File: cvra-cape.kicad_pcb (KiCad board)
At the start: 2 copper layers, 160 parts, among them Q1 MBT3904DW1T1, Q2 MBT3904DW1T1, Q3 MBT3904DW1T1, Q4 MBT3904DW1T1, Q5 MBT3904DW1T1, SW1 MicroSwitch, SW10 MicroSwitch, SW11 MicroSwitch, SW12 MicroSwitch, SW13 MicroSwitch, SW14 MicroSwitch, SW15 MicroSwitch, SW16 MicroSwitch, SW2 MicroSwitch, SW3 MicroSwitch, SW4 MicroSwitch, SW5 MicroSwitch, SW6 MicroSwitch, SW7 MicroSwitch, SW8 MicroSwitch, SW9 MicroSwitch, U1 BEAGLEBONE, U2 MCP2515_TSSOP, U3 SN65HVD256, U4 SN65HVD256, U5 BQ32000, U6 PCA9685, U7 LTC4362, X1 8Mhz, X2 32768Hz

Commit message: Place components on PCB
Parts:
- added G***: LOGO, _logo:CVRA-logo-big, F.Cu at (155.3, 103.4)
- BT1: moved to B.Cu
- U2: footprint Housings_SSOP:TSSOP-20_4.4x6.5mm_Pitch0.65mm -> _std:TSSOP20
- U6: footprint Housings_SSOP:TSSOP-28_4.4x9.7mm_Pitch0.65mm -> _std:TSSOP28
- moved R15 119.6 mm to (103.0, 71.0)
- moved C7 119.4 mm to (103.0, 68.1), turned to 180 degrees
- moved R18 117.8 mm to (106.0, 69.5)
- moved R26 116.5 mm to (109.0, 69.5)
- moved CONN7 115.4 mm to (103.0, 74.0), turned to 270 degrees
- moved R25 115.3 mm to (109.0, 71.0)
- moved C8 112.7 mm to (106.0, 68.1), turned to 180 degrees
- moved C10 112.1 mm to (112.0, 68.1), turned to 180 degrees
- moved C9 111.0 mm to (109.0, 68.1), turned to 180 degrees
- moved R17 110.5 mm to (106.0, 71.0)
- moved R28 109.3 mm to (111.9, 69.5)
- moved R16 108.1 mm to (103.0, 69.5)
- moved R33 107.5 mm to (126.9, 105.5)
- moved C12 106.9 mm to (118.0, 68.1), turned to 180 degrees
- moved C11 106.8 mm to (115.0, 68.1), turned to 180 degrees
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- renumbered CONN21 to 0, CONN22 to 1, CONN35 to 10, CONN36 to 11, CONN39 to 12, CONN23 to 2, CONN24 to 3, CONN27 to 4, CONN28 to 5, CONN29 to 6, CONN30 to 7, CONN33 to 8, CONN34 to 9
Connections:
- Q1 pad 6: Net-(Q1-Pad6) -> Net-(CONN18-Pad2)
- X2 pad 2: GND -> Net-(C16-Pad1)
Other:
- board outline added: 86.4 x 54.6 mm

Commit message: Routing
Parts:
- moved C3 8.40 mm to (114.8, 83.9), turned to 0 degrees
- moved C1 8.37 mm to (114.8, 92.3), turned to 180 degrees
- moved C10 6.10 mm to (118.0, 68.1)
- moved R27 6.10 mm to (118.0, 71.0), turned to 180 degrees
- moved R28 6.10 mm to (118.0, 69.5)
- moved CONN10 6.10 mm to (118.0, 74.0)
- moved C9 3.11 mm to (105.9, 68.1)
- moved R25 3.11 mm to (105.9, 71.0), turned to 180 degrees
- moved R26 3.11 mm to (105.9, 69.5)
- moved CONN9 3.11 mm to (105.9, 74.0)
- moved R37 3.05 mm to (114.9, 71.0), turned to 180 degrees
- moved C11 3.05 mm to (112.0, 68.1)
- moved C12 3.05 mm to (114.9, 68.1)
- moved CONN11 3.05 mm to (112.0, 74.0)
- moved R35 3.05 mm to (111.9, 71.0), turned to 180 degrees
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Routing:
- net GND: track 0.00 -> 244.4 mm, vias 0 -> 49
- net +5V: track 0.00 -> 96.0 mm, vias 0 -> 5
- net /I2C2_SCL: track 0.00 -> 93.5 mm, vias 0 -> 3
- net /I2C2_SDA: track 0.00 -> 91.0 mm, vias 0 -> 3
- net /V_CAN_BUS: track 0.00 -> 88.5 mm, vias 0 -> 6
- net /PWMGEN_OE: track 0.00 -> 49.5 mm, vias 0 -> 2
- net /CAN1_SILENT: track 0.00 -> 43.4 mm, vias 0 -> 1
- net +3V3: track 0.00 -> 42.9 mm, vias 0 -> 7
- net /D_IN_20: track 0.00 -> 42.2 mm, vias 0 -> 1
- net /Actuators/POWER: track 0.00 -> 37.6 mm
- net /D_IN_18: track 0.00 -> 36.9 mm, vias 0 -> 1
- net /D_IN_19: track 0.00 -> 36.3 mm, vias 0 -> 1
- net /D_IN_17: track 0.00 -> 34.6 mm, vias 0 -> 1
- net /SPI_CAN_MOSI: track 0.00 -> 34.2 mm, vias 0 -> 1
- net /SPI_CAN_SCK: track 0.00 -> 33.7 mm, vias 0 -> 1
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- added copper zone on F.Cu, net +3V3
- added copper zone on B.Cu, net GND
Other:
- net class Default: clearance 0.2 -> 0.15; trace_width 0.25 -> 0.2
- rule trace_clearance: 0.2 -> 0.15

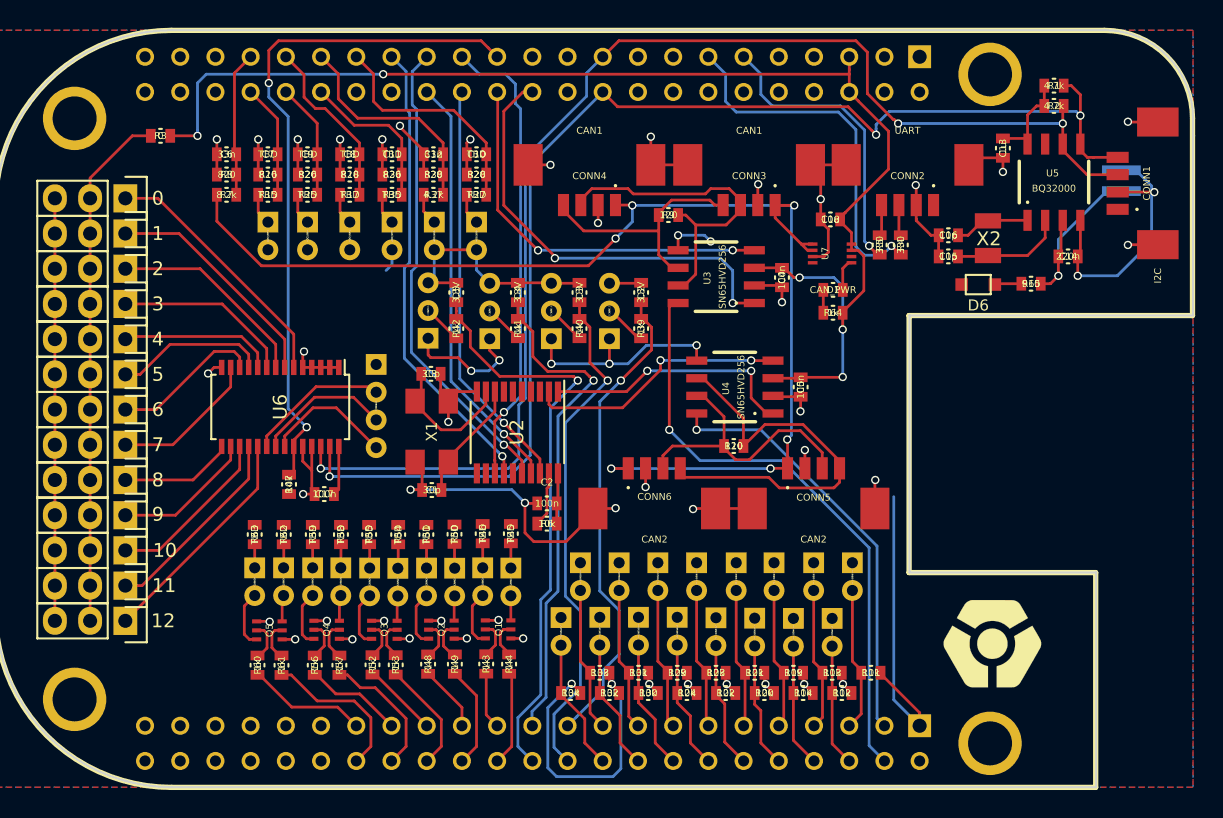
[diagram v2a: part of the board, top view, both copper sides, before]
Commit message: Routing corrections
- Use GND plane on both sides
- Route power lines as 0.5mm thickness tracks
- Cleanup crystals wiring (symetry)
- Cleanup ADC wiring to avoid crosstalk
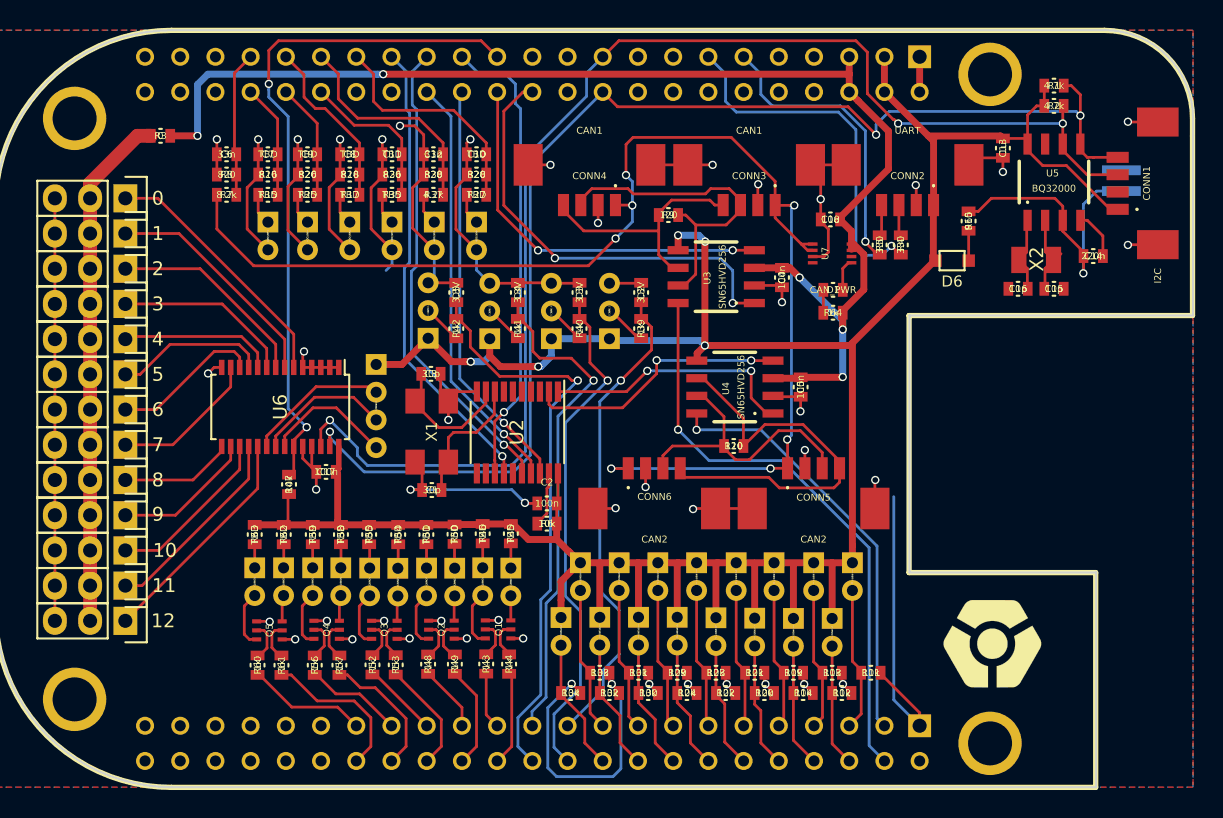
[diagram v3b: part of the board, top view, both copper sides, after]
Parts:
- moved C15 7.97 mm to (159.7, 77.8), turned to 0 degrees
- moved R65 6.38 mm to (153.5, 72.9), turned to 90 degrees
- moved C16 6.34 mm to (157.1, 77.8)
- moved X2 3.82 mm to (158.4, 75.7), turned to 180 degrees
- moved D6 2.56 mm to (152.3, 75.7)
- moved C14 1.82 mm to (162.5, 75.4)
- moved C17 1.61 mm to (107.2, 91.0)
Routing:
- net +3V3: track 42.9 -> 286.3 mm, vias 7 -> 5
- net /Actuators/POWER: track 37.6 -> 62.8 mm
- net +5V: track 96.0 -> 109.2 mm
- net GND: track 244.4 -> 253.8 mm, vias 49 -> 47
- net Net-(BT1-Pad1): track 14.2 -> 22.2 mm
- net /V_CAN_BUS: track 88.5 -> 96.1 mm, vias 6 -> 7
- net Net-(C15-Pad1): track 8.11 -> 5.74 mm
- net /I2C2_SCL: track 93.5 -> 95.0 mm
- net /CAN1_SILENT: track 43.4 -> 42.3 mm
- net Net-(C1-Pad1): track 8.69 -> 9.66 mm
- added copper zone on F.Cu, net GND
- removed copper zone on F.Cu, net +3V3
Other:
- net class Power added: clearance 0.15, trace_width 0.5, via_dia 0.6, via_drill 0.4
- net class Power+ added: clearance 0.2, trace_width 1, via_dia 0.6, via_drill 0.4

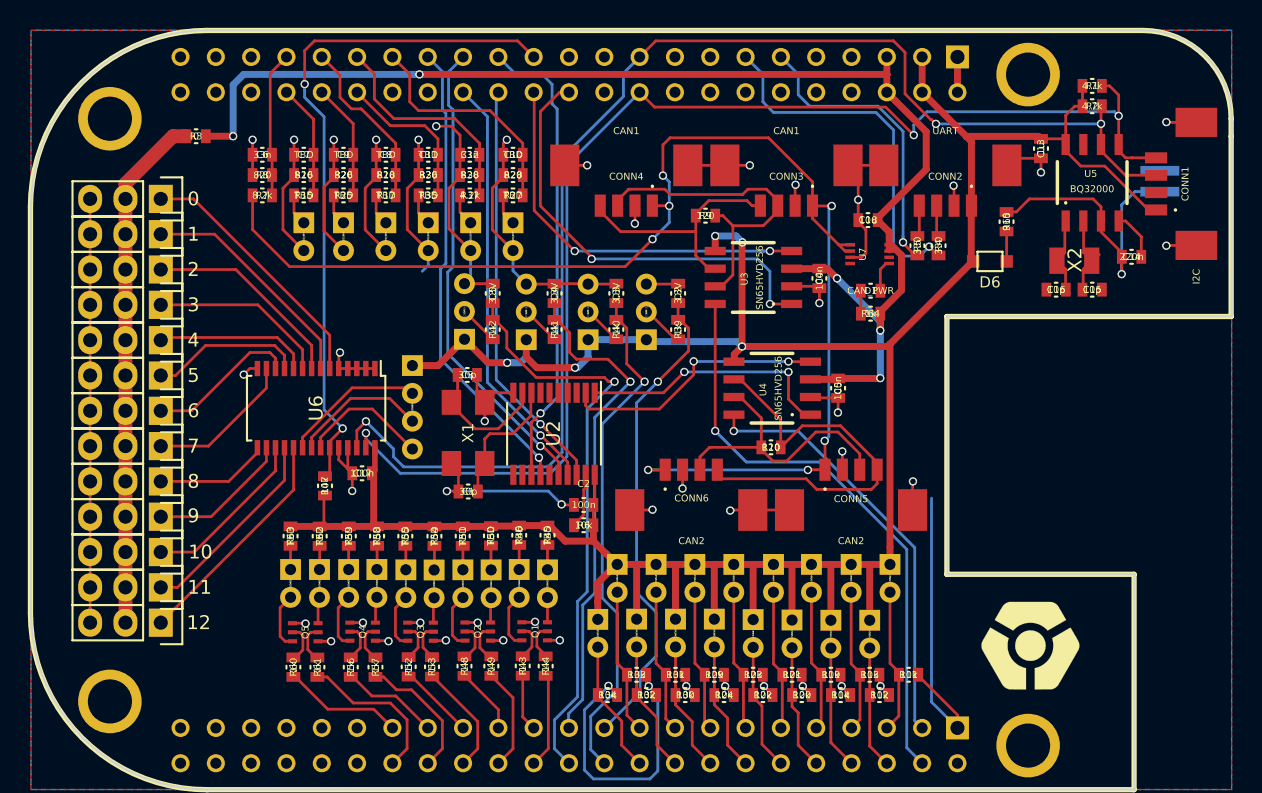
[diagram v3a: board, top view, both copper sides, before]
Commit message: Add Power connector for servos and silkscreen annotations
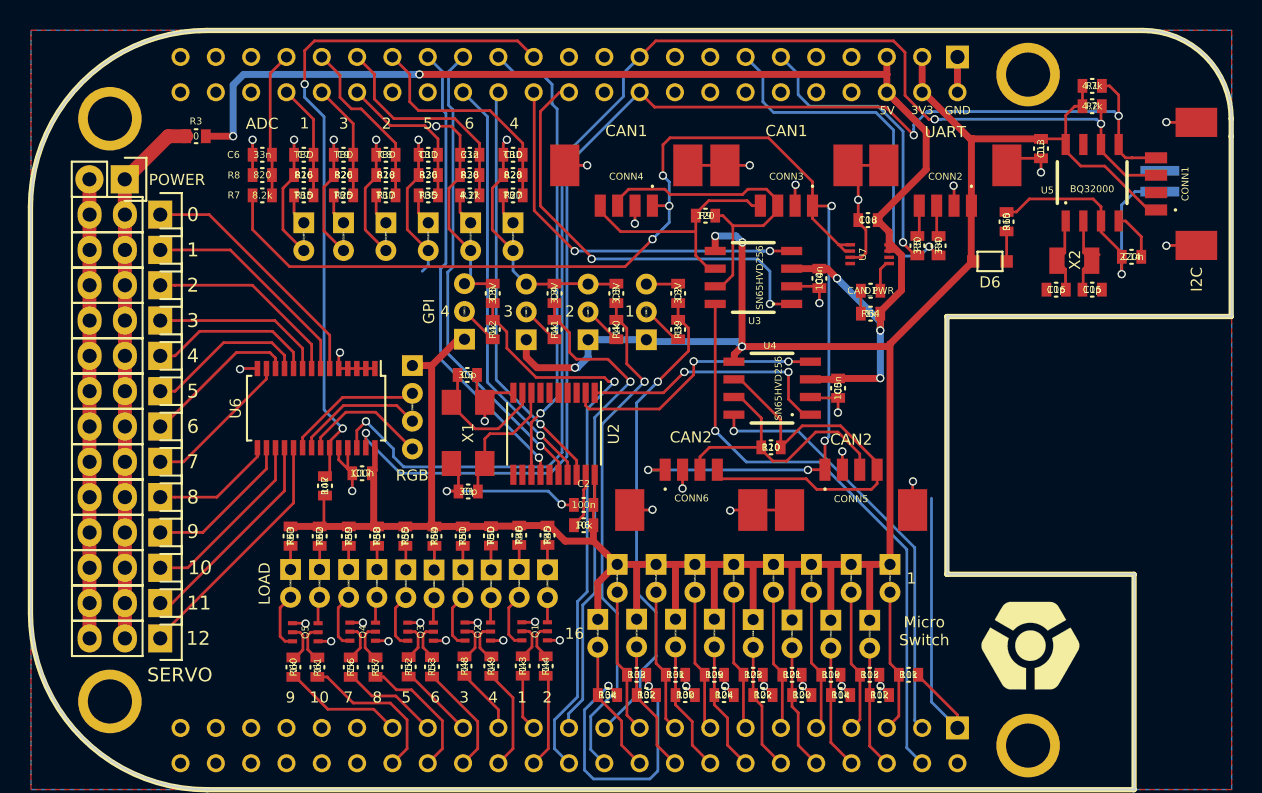
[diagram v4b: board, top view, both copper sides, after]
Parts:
- added POWER: Power Connector, Pin_Headers:Pin_Header_Straight_1x02, F.Cu at (90.1, 69.8)
- moved 0 1.13 mm to (92.7, 72.4)
- moved 11 1.13 mm to (92.7, 100.3)
- moved 2 1.13 mm to (92.7, 77.5)
- moved 4 1.13 mm to (92.7, 82.5)
- moved 6 1.13 mm to (92.7, 87.6)
- moved 7 1.13 mm to (92.7, 90.2)
- moved 8 1.13 mm to (92.7, 92.7)
- moved 9 1.13 mm to (92.7, 95.2)
- moved 1 1.13 mm to (92.7, 74.9)
- moved 10 1.13 mm to (92.7, 97.8)
- moved 12 1.13 mm to (92.7, 102.9)
- moved 3 1.13 mm to (92.7, 80.0)
- moved 5 1.13 mm to (92.7, 85.1)
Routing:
- net /Actuators/POWER: track 62.8 -> 38.8 mm
- net +3V3: track 286.3 -> 277.1 mm, vias 5 -> 4
- net GND: track 253.8 -> 256.4 mm
- net /Actuators/PWM_12: track 16.5 -> 17.7 mm
- net /Actuators/PWM_11: track 14.4 -> 15.4 mm
- net /Actuators/PWM_4: track 11.2 -> 12.1 mm
- net /Actuators/PWM_10: track 12.3 -> 13.2 mm
- net /Actuators/PWM_9: track 10.2 -> 11.0 mm
- net /Actuators/PWM_8: track 8.16 -> 8.83 mm
- net /Actuators/PWM_5: track 11.0 -> 11.7 mm
- net /Actuators/PWM_6: track 10.9 -> 11.4 mm
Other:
- board text added: "1"
- board text added: "10"
- board text added: "16"
- board text added: "2"
- board text added: "3"
- board text added: "3V3"
- board text added: "4"
- board text added: "5"
- board text added: "5V"
- board text added: "6"
- board text added: "7"
- board text added: "8"
- board text added: "9"
- board text added: "ADC"
- board text added: "CVRA Cape Rev A March 2016"
- board text added: "GND"
- board text added: "GPI"
- board text added: "LOAD"
- board text added: "Micro Switch"
- board text added: "RGB"
- board text added: "SERVO"
